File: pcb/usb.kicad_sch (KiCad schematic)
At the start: 4 parts, among them J2 Connector, USB-TYPE-C-16P

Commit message: sch: replace mcu and clean up schematic
Fixes #27
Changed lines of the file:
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@@
 	)
 	(hierarchical_label "{USB}"
-		(shape input)
+		(shape bidirectional)
 		(at 82.55 30.48 0)
 		(effects

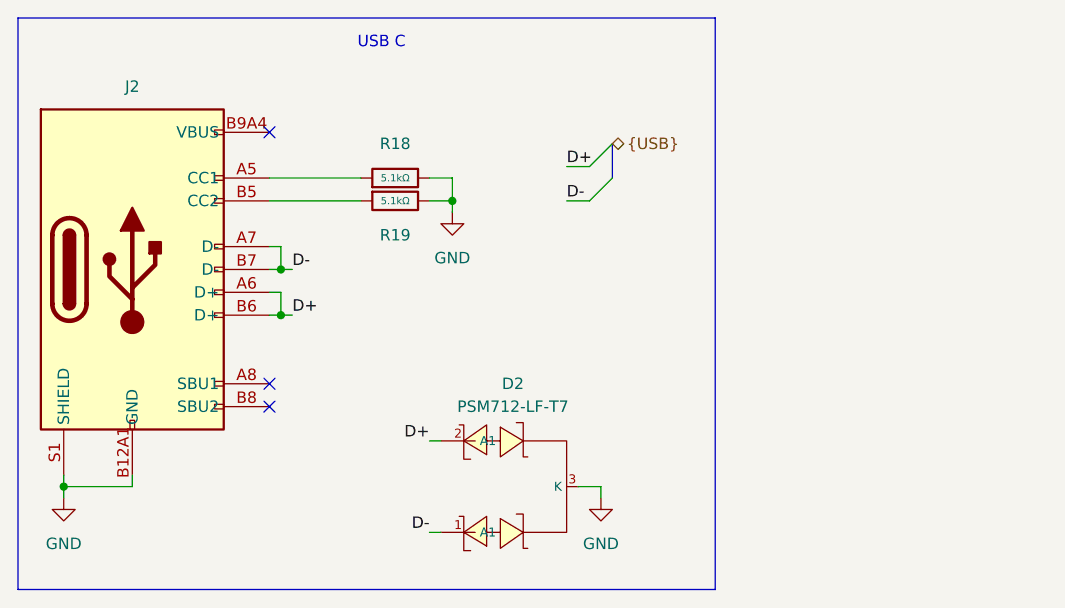
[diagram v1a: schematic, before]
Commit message: sch: switch to vertical usb c and replace esd ic
This replaces the existing edge-mount USB C connector for a vertical one to ease routing and placement. Also swaps the unsuitable ESD IC with a specific USB ESD protection IC. Relates to #1
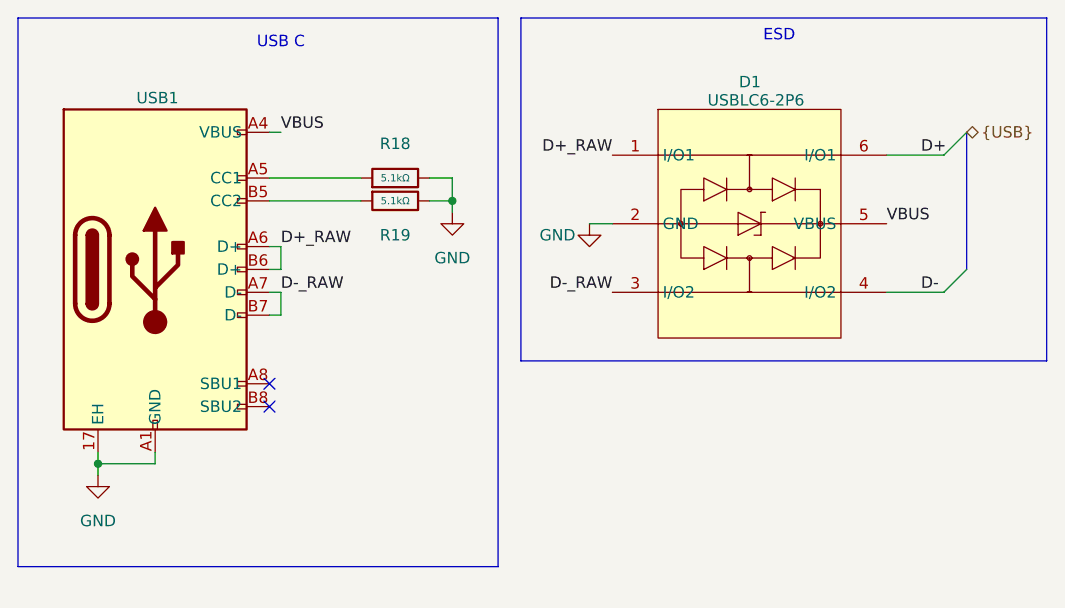
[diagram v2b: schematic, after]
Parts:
- removed D2: PSM712-LF-T7, PCM_JLCPCB:SOT-23-3_L3.0-W1.7-P0.95-LS2.9-BR, symbol EasyEDA:TVS-Bi,_PSM712-LF-T7
- removed J2: Connector, USB-TYPE-C-16P, PCM_JLCPCB:TYPE-C-SMD_HX-TYPE-C-16PIN, symbol PCM_JLCPCB-Extended:Connector, USB-TYPE-C-16P
- added D1: USBLC6-2P6, EasyEDA:SOT-666-6_L1.6-W1.2-P0.50-LS1.6-BR, symbol EasyEDA:USBLC6-2P6
- added USB1: GT-USB-7055BB, EasyEDA:USB-C-TH_GT-USB-7055BB, symbol EasyEDA:GT-USB-7055BB
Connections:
- net D+: now also D1.6 (I/O1)
- net D-: now also D1.4 (I/O2)
- net GND: now also D1.2 (GND), USB1.17 (EH), USB1.A1 (GND), USB1.A12 (GND), USB1.B1 (GND), USB1.B12 (GND)
- net at R19.1: now also USB1.B5 (CC2)
- net at R18.1: now also USB1.A5 (CC1)
- new net D+_RAW: D1.1 (I/O1), USB1.A6 (D+), USB1.B6 (D+)
- new net D-_RAW: D1.3 (I/O2), USB1.A7 (D-), USB1.B7 (D-)
- new net VBUS: D1.5 (VBUS), USB1.A4 (VBUS), USB1.A9 (VBUS), USB1.B4 (VBUS), USB1.B9 (VBUS)
- no-connect marks 3 -> 2
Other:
- note added: "ESD"

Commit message: sch: add schematic titles and do some cleanup
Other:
- company: (none) -> CIA Assured
- title: (none) -> USB Programming Interface
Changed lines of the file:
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@@
 	(generator_version "10.0")
 	(paper "A4")
+	(title_block
+		(title "USB Programming Interface")
+		(company "CIA Assured")
+	)
 	(rectangle
 		(start 16.51 16.51)
